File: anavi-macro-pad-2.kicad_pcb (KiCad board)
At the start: 2 copper layers, 40.6 x 38 mm, 22 parts, among them J1 USB_B_Micro, K1 SW_DIP_x01, K2 SW_DIP_x01, Q1 Q_NPN_BEC, U1 ATtiny85-20SU

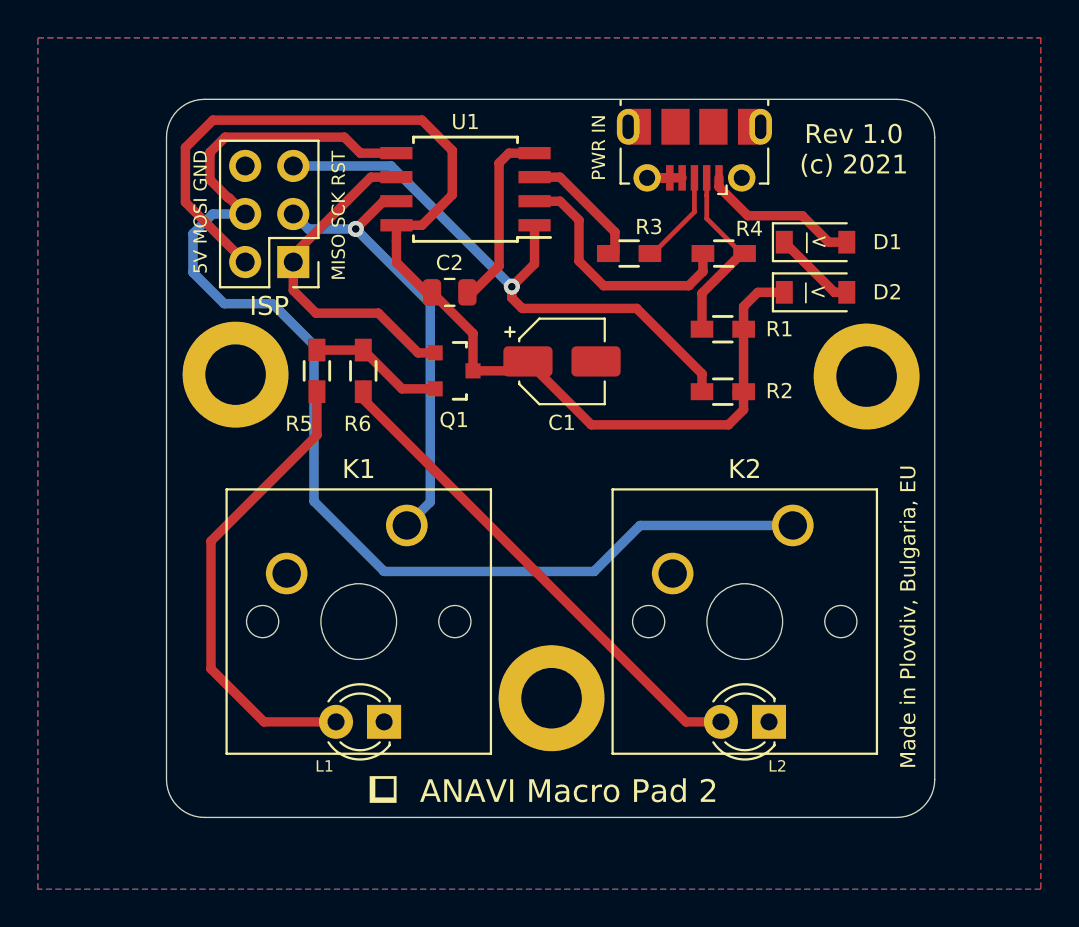
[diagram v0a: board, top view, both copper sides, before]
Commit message: anavi-macro-pad-2.kicad_pcb: Update silkscreen
Update the silkscreen:

- Replace 5V with VCC on the ISP connector because if measured
  when the board is booted from the microUSB it will be about
  3.6-3.7V because of diodes D1 and D2.
- Remove the white frames around the keys
- Replace labels K1 and K2 with KEY 1 and KEY 2
- Increse size and adjust positions of L1 and L2 labels

Signed-off-by: Leon Anavi <leon@anavi.org>
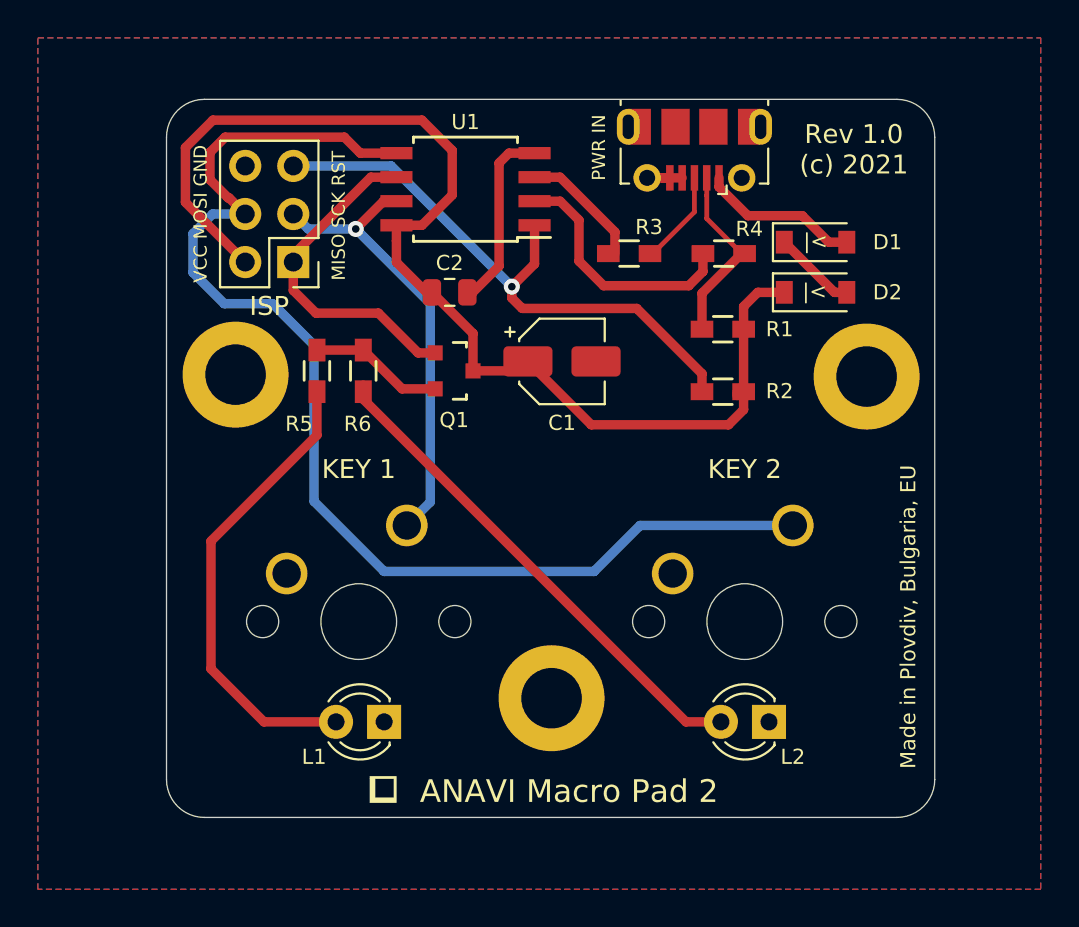
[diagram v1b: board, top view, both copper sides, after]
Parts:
- KEY 1: renamed from K1
- KEY 2: renamed from K2
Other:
- board text added: "VCC MOSI GND"
- board text removed: "5V MOSI GND"
